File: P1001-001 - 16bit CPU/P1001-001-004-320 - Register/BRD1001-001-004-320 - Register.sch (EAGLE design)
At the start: 20 parts, among them IC1 74HC173D, IC12 74AC245DW, IC2 74HC173D, IC27 MEGA8535-A, IC3 74HC173D, IC4 74HC173D, IC7 74AC245DW, J1 22-27-2041-04, J3 22-27-2041-04, J4 22-27-2061-06

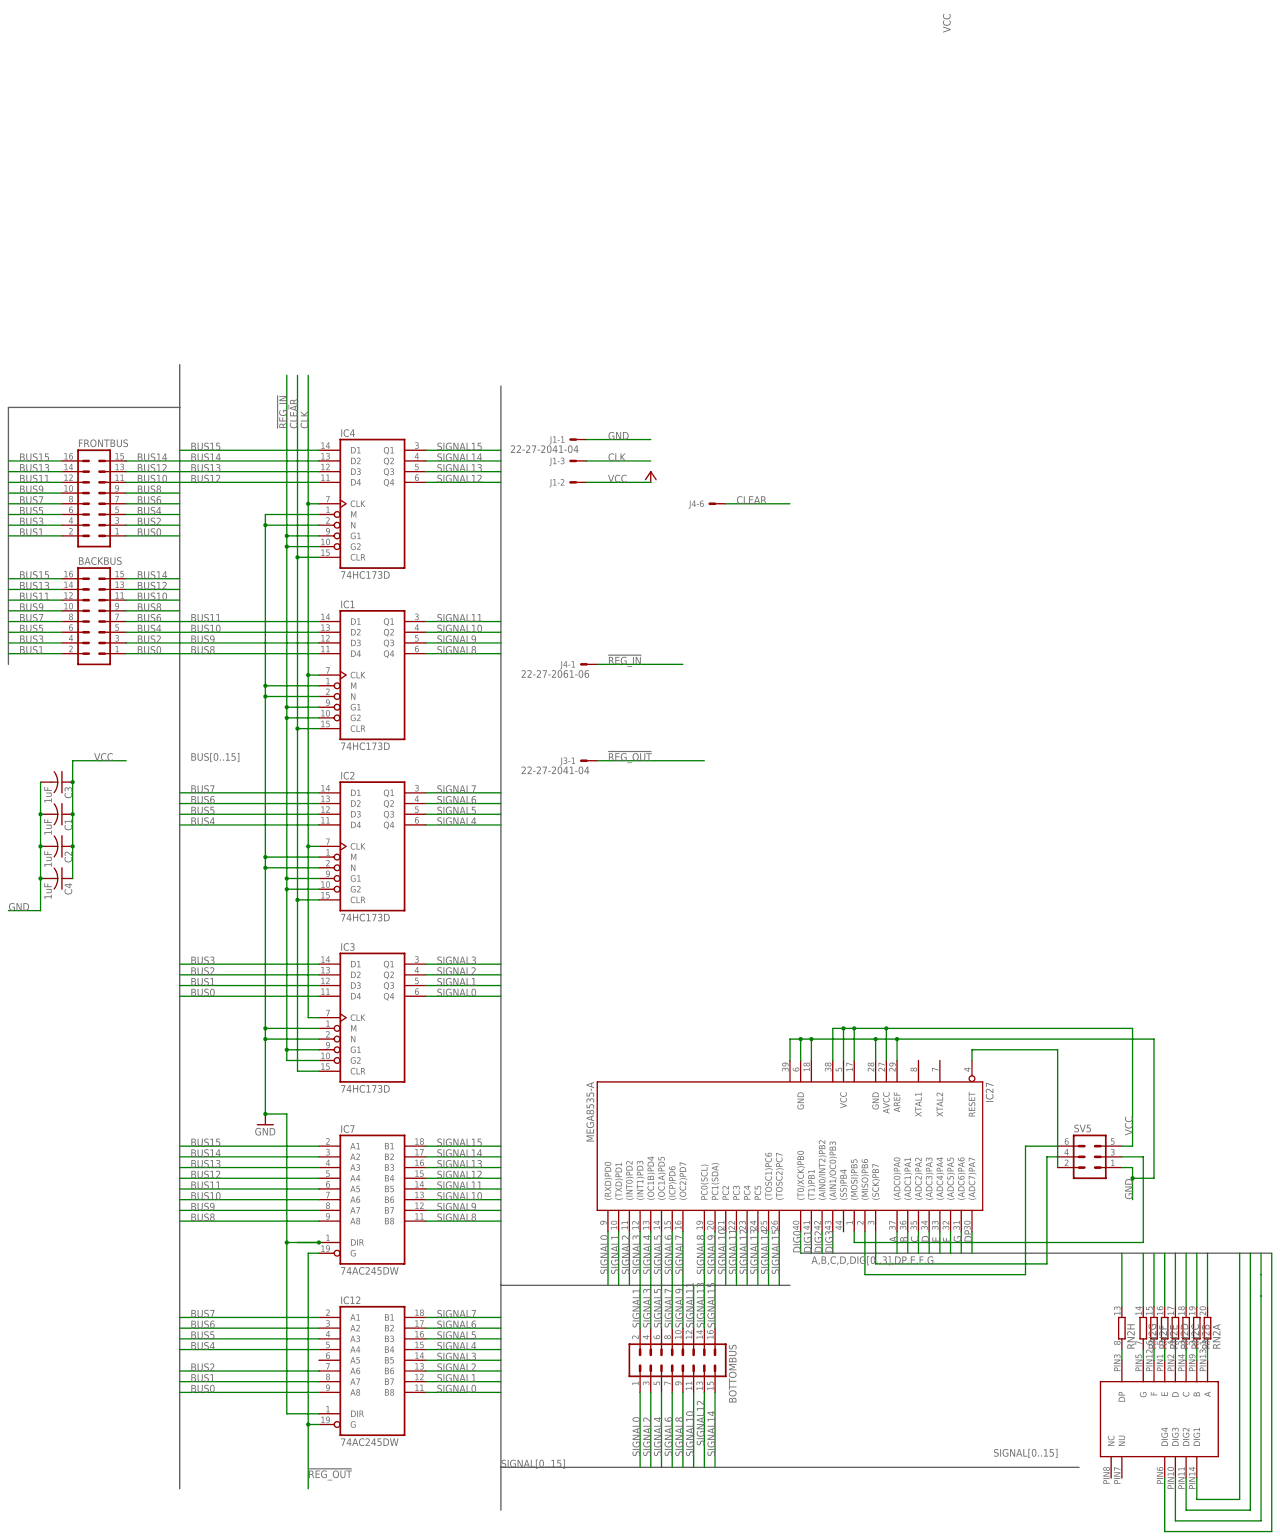
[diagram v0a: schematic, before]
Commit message: add ram to Memory
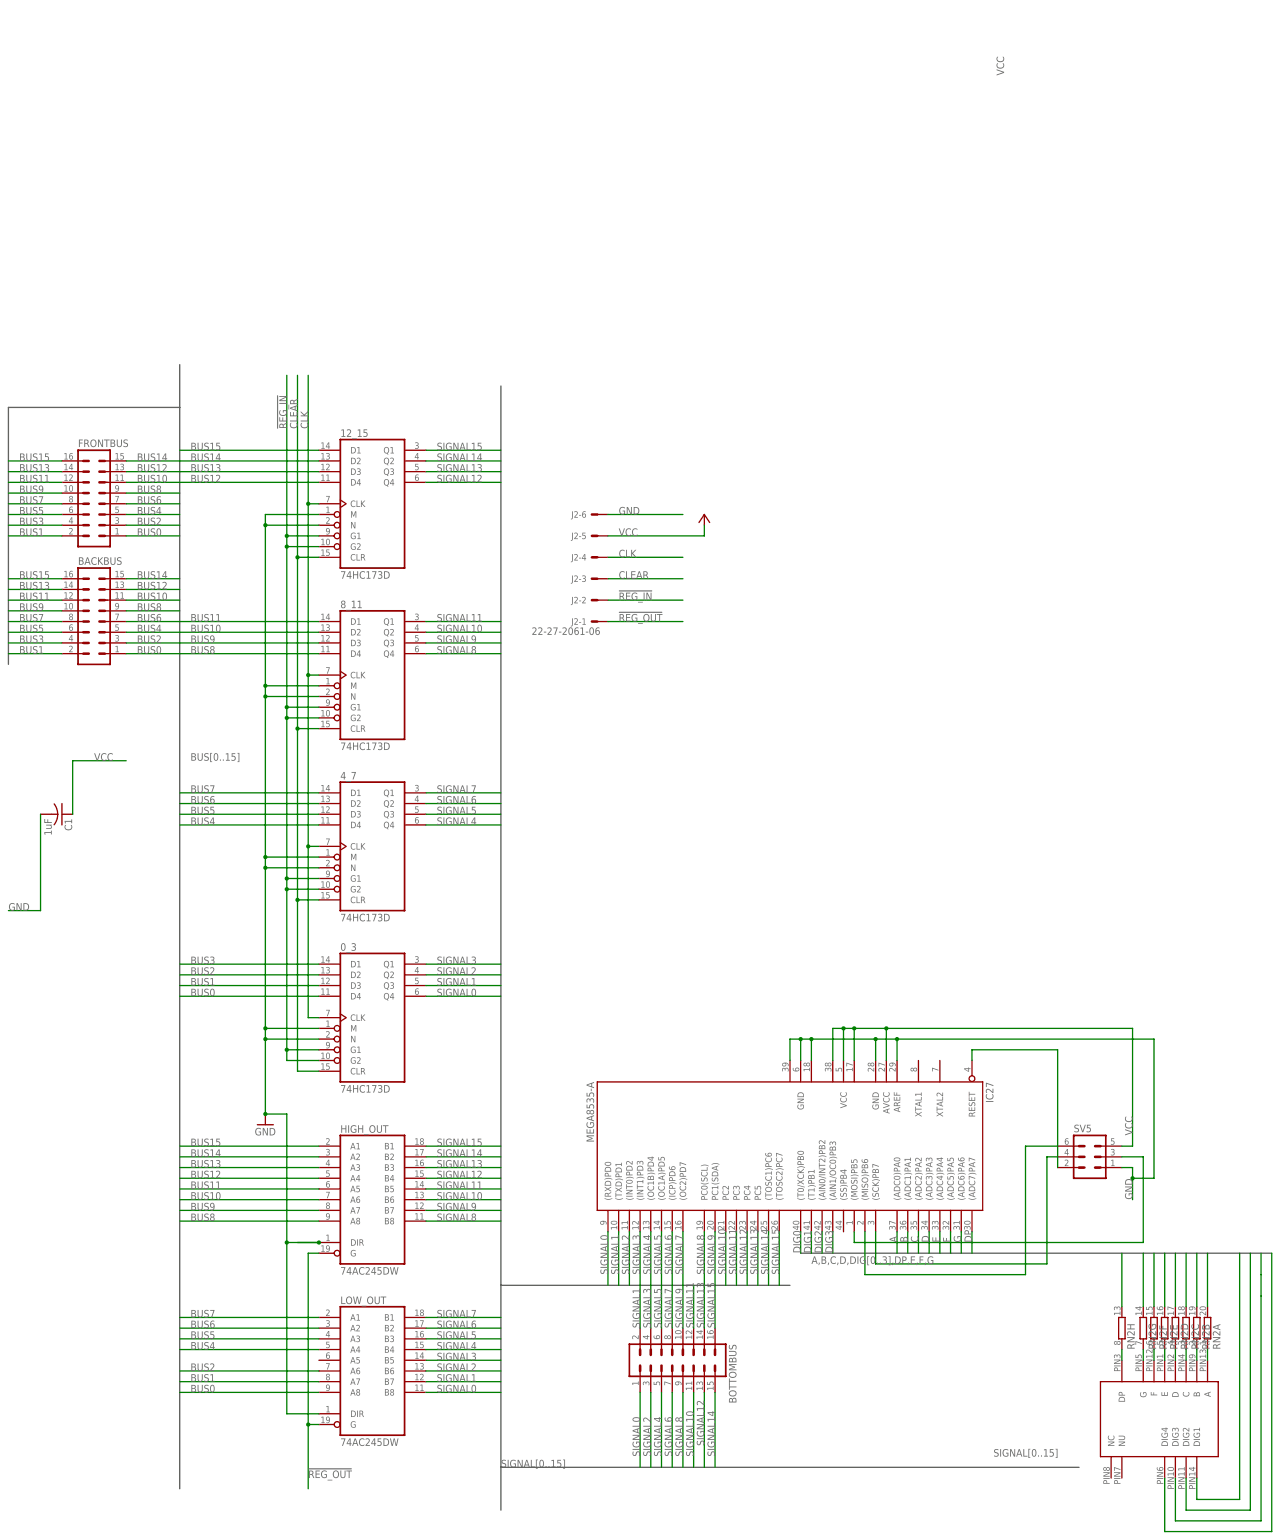
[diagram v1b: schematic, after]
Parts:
- removed C2, C3, C4: 1uF, rcl:C-USC1206
- removed J1, J3: 22-27-2041-04, con-molex:22-27-2041-04
- removed J4: 22-27-2061-06, con-molex:22-27-2061-06
- added J2: 22-27-2061-06, con-molex:22-27-2061-06
- renumbered IC1 to 8_11, IC12 to LOW_OUT, IC2 to 4_7, IC3 to 0_3, IC4 to 12_15, IC7 to HIGH_OUT
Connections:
- net !REG_IN: now also J2-2.S; no longer J4-1.S
- net !REG_OUT: now also J2-1.S; no longer J3-1.S
- net CLEAR: now also J2-3.S; no longer J4-6.S
- net CLK: now also J2-4.S; no longer J1-3.S
- net GND: now also J2-6.S; no longer C2.2, C3.2, C4.2, J1-1.S
- net VCC: now also J2-5.S; no longer C2.1, C3.1, C4.1, J1-2.S
